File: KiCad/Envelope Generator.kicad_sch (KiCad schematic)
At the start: 36 parts, among them U10 TL074, U9 TL074

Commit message: routed the filter, updated 0201 footprints to 0402
JLCPCB's economy PCBA has a footprint bottom limit of 0402 imperial
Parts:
- R54, R55, R57, R58, R59, R63, R64, R65: footprint Resistor_SMD:R_0201_0603Metric -> Resistor_SMD:R_0402_1005Metric
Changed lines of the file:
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@@
 			)
 		)
-		(property "Footprint" "Resistor_SMD:R_0201_0603Metric"
+		(property "Footprint" "Resistor_SMD:R_0402_1005Metric"
 			(at 50.546 96.774 90)
 			(hide yes)
@@
 			)
 		)
-		(property "Footprint" "Resistor_SMD:R_0201_0603Metric"
+		(property "Footprint" "Resistor_SMD:R_0402_1005Metric"
 			(at 89.916 152.654 90)
 			(hide yes)
@@
 			)
 		)
-		(property "Footprint" "Resistor_SMD:R_0201_0603Metric"
+		(property "Footprint" "Resistor_SMD:R_0402_1005Metric"
 			(at 48.514 40.894 90)
 			(hide yes)
@@
 			)
 		)
-		(property "Footprint" "Resistor_SMD:R_0201_0603Metric"
+		(property "Footprint" "Resistor_SMD:R_0402_1005Metric"
 			(at 35.306 96.774 90)
 			(hide yes)
@@
 			)
 		)
-		(property "Footprint" "Resistor_SMD:R_0201_0603Metric"
+		(property "Footprint" "Resistor_SMD:R_0402_1005Metric"
 			(at 50.546 152.654 90)
 			(hide yes)
@@
 			)
 		)
-		(property "Footprint" "Resistor_SMD:R_0201_0603Metric"
+		(property "Footprint" "Resistor_SMD:R_0402_1005Metric"
 			(at 38.354 40.894 90)
 			(hide yes)
@@
 			)
 		)
-		(property "Footprint" "Resistor_SMD:R_0201_0603Metric"
+		(property "Footprint" "Resistor_SMD:R_0402_1005Metric"
 			(at 89.916 96.774 90)
 			(hide yes)
@@
 			)
 		)
-		(property "Footprint" "Resistor_SMD:R_0201_0603Metric"
+		(property "Footprint" "Resistor_SMD:R_0402_1005Metric"
 			(at 35.306 152.654 90)
 			(hide yes)

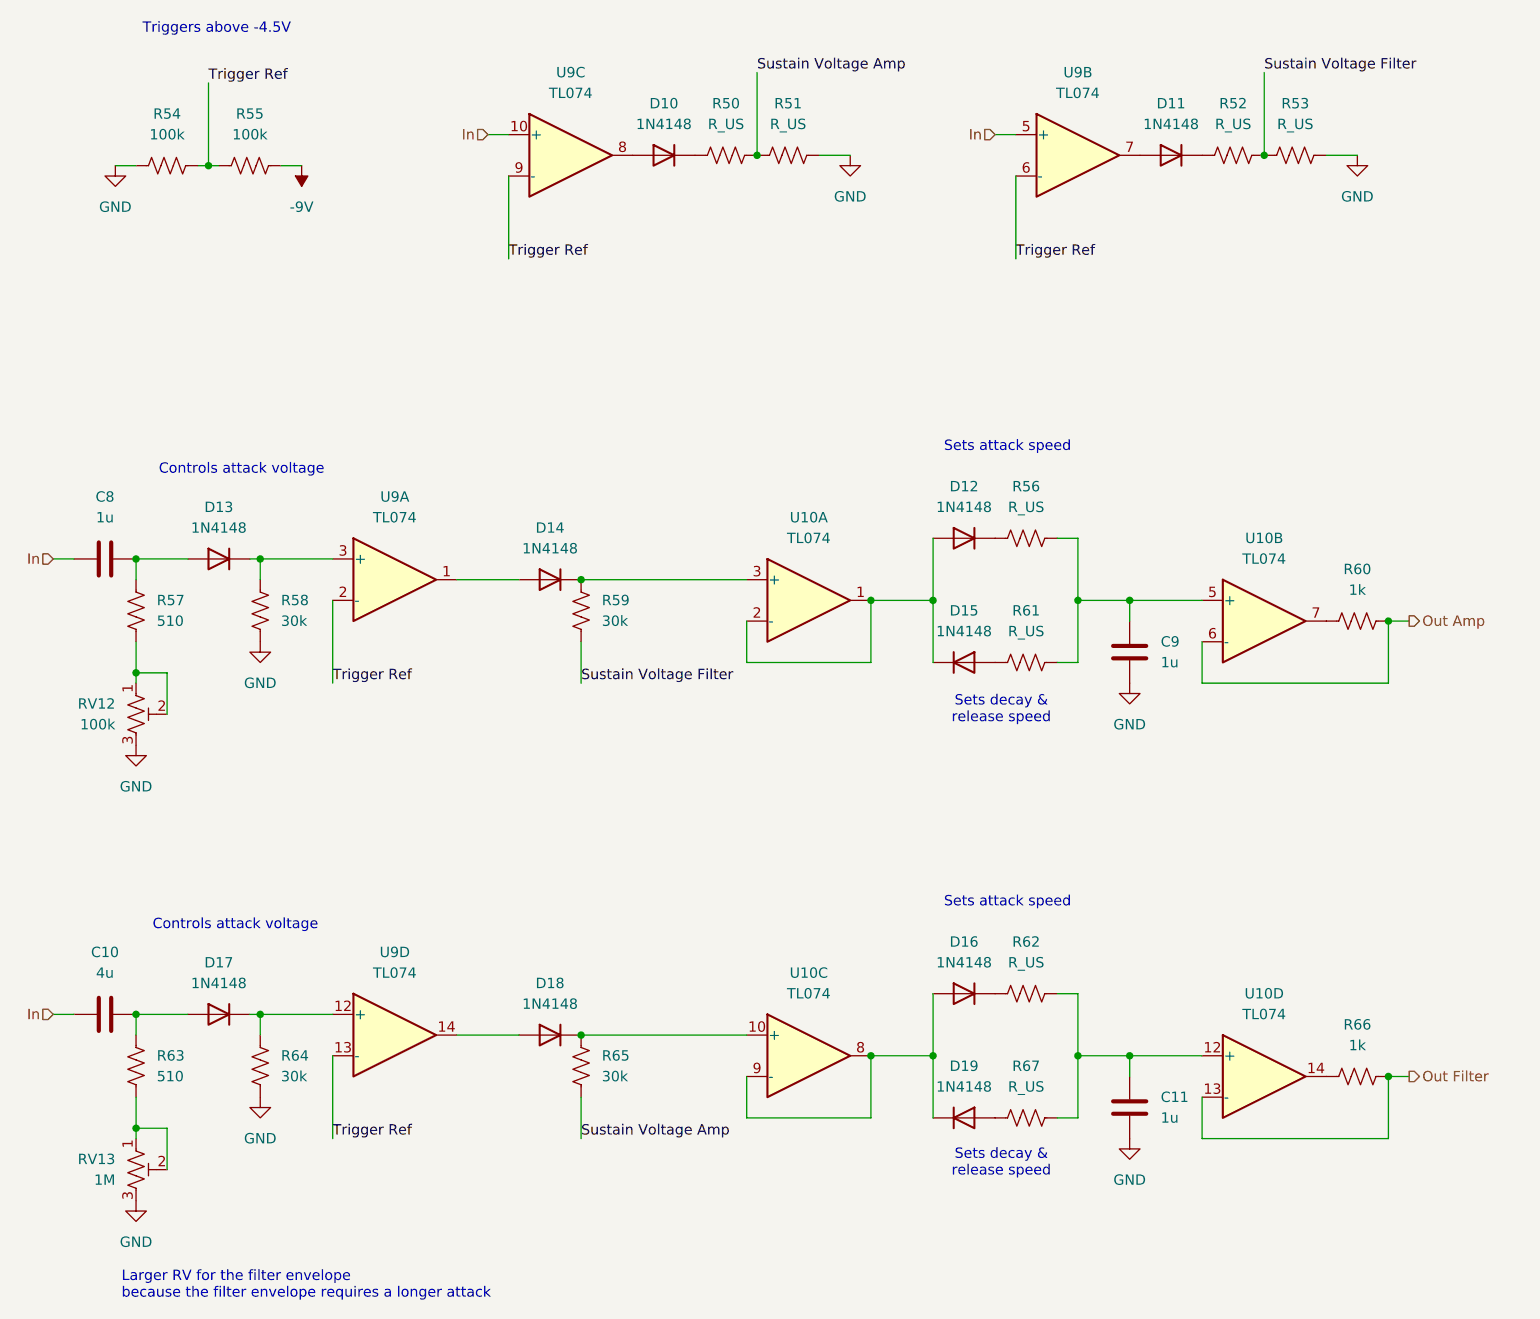
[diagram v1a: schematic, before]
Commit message: placed and routed envelope core
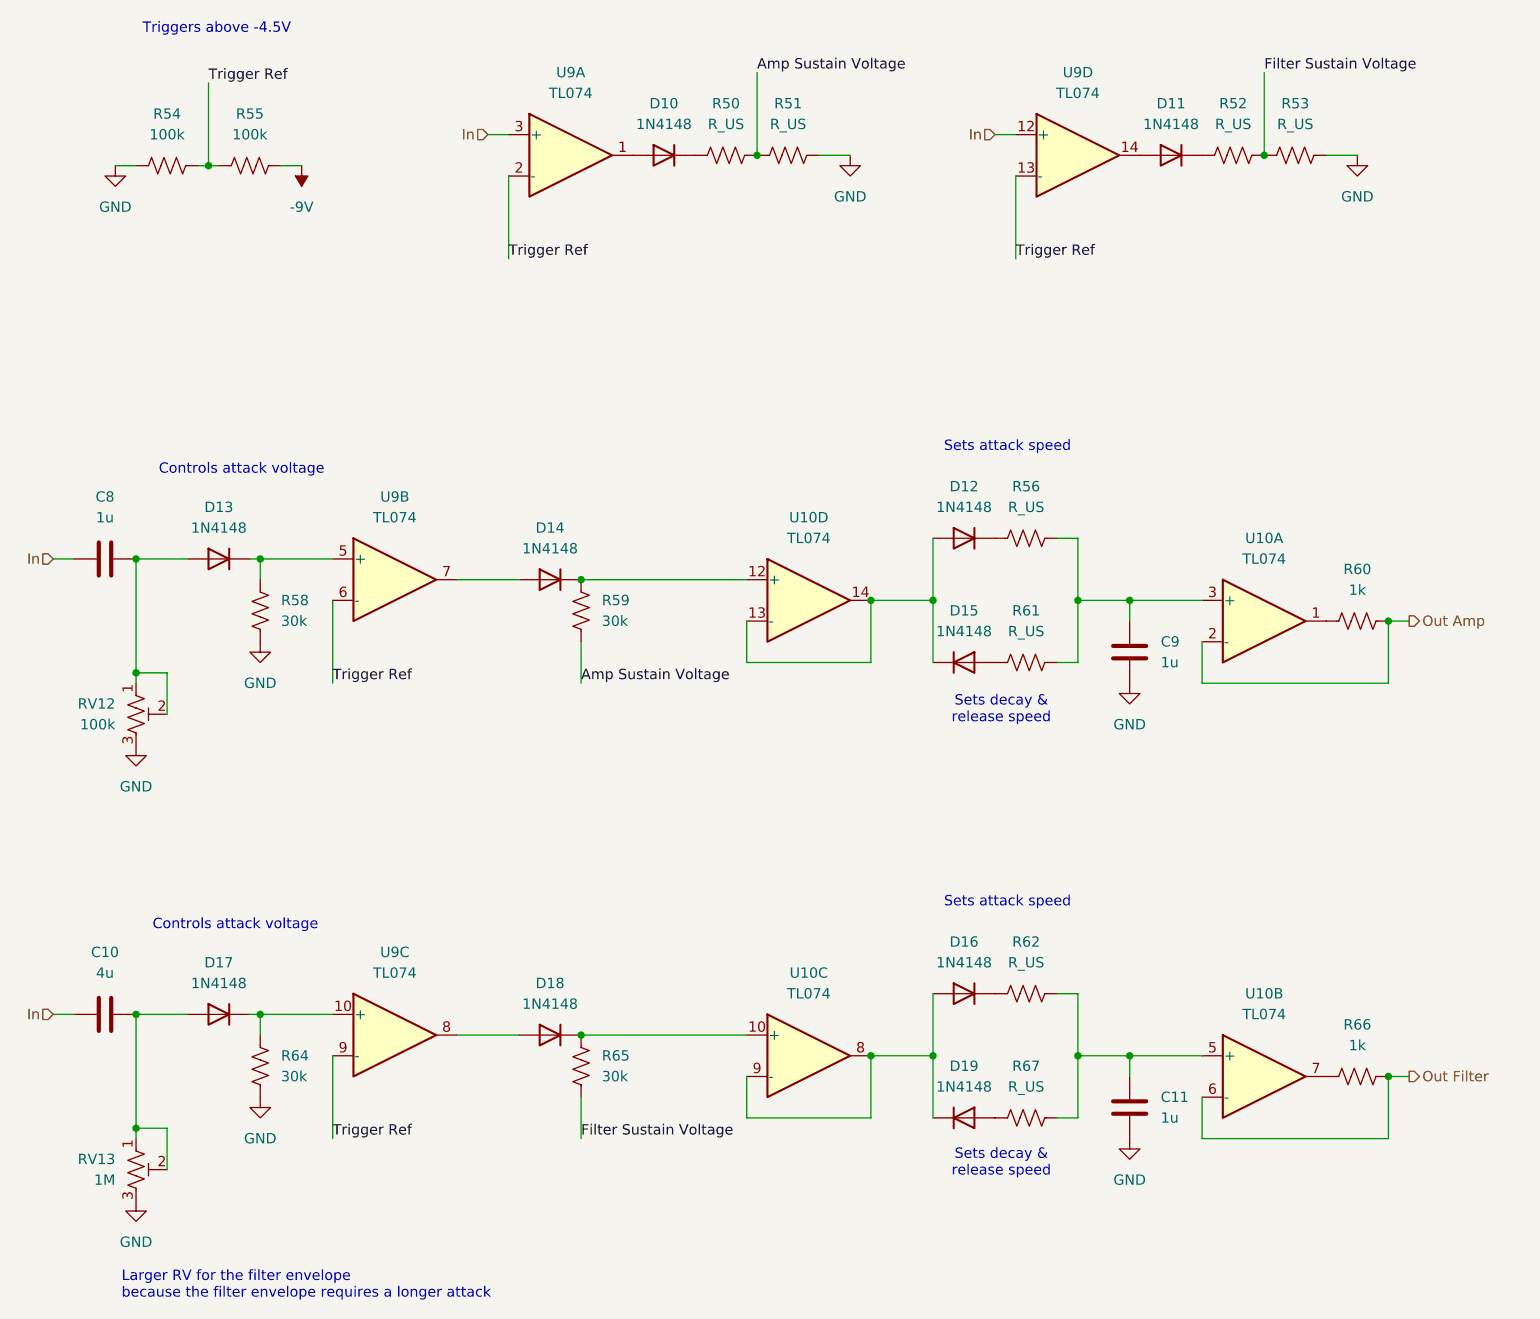
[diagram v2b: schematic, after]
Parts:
- removed R57, R63: 510, Resistor_SMD:R_0402_1005Metric, symbol Device:R_US
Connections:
- net In: now also U9.12 (+), U9.3 (+); no longer U9.10 (+), U9.5 (+)
- net Out Amp: now also U10.2 (-); no longer U10.6 (-)
- net Out Filter: now also U10.6 (-); no longer U10.13 (-)
- net Trigger Ref: now also U9.13 (-), U9.2 (-), U9.6 (-), U9.9 (-); no longer U9.13 (-), U9.2 (-), U9.6 (-), U9.9 (-)
- net at C11.2, R62.2, R67.2: now also U10.5 (+); no longer U10.12 (+)
- net at C9.2, R56.2, R61.2: now also U10.3 (+); no longer U10.5 (+)
- net at C10.2, D17.2 (A): now also RV13.1, RV13.2
- net at D18.2 (A): now also U9.8; no longer U9.14
- net at D10.2 (A): now also U9.1; no longer U9.8
- net at R66.1: now also U10.7; no longer U10.14
- net at D13.1 (K), R58.1: now also U9.5 (+); no longer U9.3 (+)
- net at D12.2 (A), D15.1 (K): now also U10.13 (-), U10.14; no longer U10.1, U10.2 (-)
- net at C8.2, D13.2 (A): now also RV12.1, RV12.2
- net at D17.1 (K), R64.1: now also U9.10 (+); no longer U9.12 (+)
- net at R60.1: now also U10.1; no longer U10.7
- net at D14.1 (K), R59.1: now also U10.12 (+); no longer U10.3 (+)
- net at D14.2 (A): now also U9.7; no longer U9.1
- net at D11.2 (A): now also U9.14; no longer U9.7
- net Sustain Voltage Amp renamed Amp Sustain Voltage
- net Amp Sustain Voltage: now also R59.2; no longer R65.2
- net Sustain Voltage Filter renamed Filter Sustain Voltage
- net Filter Sustain Voltage: now also R65.2; no longer R59.2
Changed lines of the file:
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@@
 	)
 	(junction
-		(at 34.29 104.14)
+		(at 149.86 151.13)
 		(diameter 0)
 		(color 0 0 0 0)
 	)
 	(junction
-		(at 149.86 151.13)
+		(at 88.9 148.59)
 		(diameter 0)
 		(color 0 0 0 0)
 	)
 	(junction
-		(at 88.9 148.59)
+		(at 132.08 151.13)
 		(diameter 0)
 		(color 0 0 0 0)
 	)
 	(junction
-		(at 132.08 151.13)
+		(at 34.29 104.14)
 		(diameter 0)
 		(color 0 0 0 0)
@@
 	(wire
 		(pts
-			(xy 34.29 148.59) (xy 34.29 146.05)
-		)
-		(stroke
-			(width 0)
-			(type default)
-		)
-	)
-	(wire
-		(pts
 			(xy 156.21 151.13) (xy 165.1 151.13)
 		)
@@
 	(wire
 		(pts
-			(xy 34.29 92.71) (xy 34.29 90.17)
+			(xy 34.29 146.05) (xy 34.29 160.02)
+		)
+		(stroke
+			(width 0)
+			(type default)
+		)
+	)
+	(wire
+		(pts
+			(xy 34.29 90.17) (xy 34.29 104.14)
 		)
 		(stroke
@@
 	(wire
 		(pts
-			(xy 34.29 100.33) (xy 34.29 104.14)
-		)
-		(stroke
-			(width 0)
-			(type default)
-		)
-	)
-	(wire
-		(pts
 			(xy 34.29 160.02) (xy 34.29 161.29)
 		)
@@
 	(wire
 		(pts
-			(xy 34.29 156.21) (xy 34.29 160.02)
-		)
-		(stroke
-			(width 0)
-			(type default)
-		)
-	)
-	(wire
-		(pts
 			(xy 149.86 95.25) (xy 149.86 102.87)
 		)
@@
 		)
 	)
-	(label "Sustain Voltage Amp"
-		(at 88.9 161.29 0)
+	(label "Trigger Ref"
+		(at 142.24 53.34 0)
 		(effects
 			(font
@@
 	)
 	(label "Trigger Ref"
-		(at 142.24 53.34 0)
+		(at 80.01 53.34 0)
 		(effects
 			(font
@@
 		)
 	)
-	(label "Sustain Voltage Amp"
-		(at 110.49 30.48 0)
+	(label "Amp Sustain Voltage"
+		(at 88.9 105.41 0)
 		(effects
 			(font
@@
 		)
 	)
-	(label "Trigger Ref"
-		(at 80.01 53.34 0)
+	(label "Filter Sustain Voltage"
+		(at 88.9 161.29 0)
 		(effects
 			(font
@@
 		)
 	)
-	(label "Sustain Voltage Filter"
-		(at 88.9 105.41 0)
+	(label "Amp Sustain Voltage"
+		(at 110.49 30.48 0)
 		(effects
 			(font
@@
 		)
 	)
-	(label "Sustain Voltage Filter"
+	(label "Filter Sustain Voltage"
 		(at 172.72 30.48 0)
 		(effects
@@
 		(lib_id "Amplifier_Operational:TL074")
 		(at 87.63 40.64 0)
-		(unit 3)
+		(unit 1)
 		(body_style 1)
 		(exclude_from_sim no)
@@
 				(path "/931827f3-33b7-460f-8885-7db258da2648/77fe3443-32fb-46cd-8502-6f8d1ae6ff63"
 					(reference "U9")
-					(unit 3)
+					(unit 1)
 				)
 			)
@@
 		(lib_id "Amplifier_Operational:TL074")
 		(at 172.72 153.67 0)
-		(unit 4)
+		(unit 2)
 		(body_style 1)
 		(exclude_from_sim no)
@@
 				(path "/931827f3-33b7-460f-8885-7db258da2648/77fe3443-32fb-46cd-8502-6f8d1ae6ff63"
 					(reference "U10")
-					(unit 4)
+					(unit 2)
 				)
 			)
@@
 	(symbol
 		(lib_id "Device:R_US")
-		(at 34.29 96.52 0)
-		(unit 1)
-		(body_style 1)
-		(exclude_from_sim no)
-		(in_bom yes)
-		(on_board yes)
-		(in_pos_files yes)
-		(dnp no)
-		(fields_autoplaced yes)
-		(property "Reference" "R57"
-			(at 36.83 95.2499 0)
-			(show_name no)
-			(do_not_autoplace no)
-			(effects
-				(font
-					(size 1.27 1.27)
-				)
-				(justify left)
-			)
-		)
-		(property "Value" "510"
-			(at 36.83 97.7899 0)
-			(show_name no)
-			(do_not_autoplace no)
-			(effects
-				(font
-					(size 1.27 1.27)
-				)
-				(justify left)
-			)
-		)
-		(property "Footprint" "Resistor_SMD:R_0402_1005Metric"
-			(at 35.306 96.774 90)
-			(hide yes)
-			(show_name no)
-			(do_not_autoplace no)
-			(effects
-				(font
-					(size 1.27 1.27)
-				)
-			)
-		)
-		(property "Datasheet" ""
-			(at 34.29 96.52 0)
-			(hide yes)
-			(show_name no)
-			(do_not_autoplace no)
-			(effects
-				(font
-					(size 1.27 1.27)
-				)
-			)
-		)
-		(property "Description" "Resistor, US symbol"
-			(at 34.29 96.52 0)
-			(hide yes)
-			(show_name no)
-			(do_not_autoplace no)
-			(effects
-				(font
-					(size 1.27 1.27)
-				)
-			)
-		)
-		(pin "2"
-		)
-		(pin "1"
-		)
-		(instances
-			(project "Electronic Trombone"
-				(path "/931827f3-33b7-460f-8885-7db258da2648/77fe3443-32fb-46cd-8502-6f8d1ae6ff63"
-					(reference "R57")
-					(unit 1)
-				)
-			)
-		)
-	)
-	(symbol
-		(lib_id "Device:R_US")
 		(at 49.53 152.4 0)
 		(unit 1)
@@
 		(lib_id "Amplifier_Operational:TL074")
 		(at 172.72 97.79 0)
-		(unit 2)
+		(unit 1)
 		(body_style 1)
 		(exclude_from_sim no)
@@
 				(path "/931827f3-33b7-460f-8885-7db258da2648/77fe3443-32fb-46cd-8502-6f8d1ae6ff63"
 					(reference "U10")
-					(unit 2)
+					(unit 1)
 				)
 			)
@@
 		(lib_id "Amplifier_Operational:TL074")
 		(at 149.86 40.64 0)
-		(unit 2)
+		(unit 4)
 		(body_style 1)
 		(exclude_from_sim no)
@@
 				(path "/931827f3-33b7-460f-8885-7db258da2648/77fe3443-32fb-46cd-8502-6f8d1ae6ff63"
 					(reference "U9")
-					(unit 2)
+					(unit 4)
 				)
 			)
@@
 		(lib_id "Amplifier_Operational:TL074")
 		(at 66.04 148.59 0)
-		(unit 4)
+		(unit 3)
 		(body_style 1)
 		(exclude_from_sim no)
@@
 				(path "/931827f3-33b7-460f-8885-7db258da2648/77fe3443-32fb-46cd-8502-6f8d1ae6ff63"
 					(reference "U9")
-					(unit 4)
+					(unit 3)
 				)
 			)
@@
 	)
 	(symbol
-		(lib_id "Device:R_US")
-		(at 34.29 152.4 0)
-		(unit 1)
-		(body_style 1)
-		(exclude_from_sim no)
-		(in_bom yes)
-		(on_board yes)
-		(in_pos_files yes)
-		(dnp no)
-		(fields_autoplaced yes)
-		(property "Reference" "R63"
-			(at 36.83 151.1299 0)
-			(show_name no)
-			(do_not_autoplace no)
-			(effects
-				(font
-					(size 1.27 1.27)
-				)
-				(justify left)
-			)
-		)
-		(property "Value" "510"
-			(at 36.83 153.6699 0)
-			(show_name no)
-			(do_not_autoplace no)
-			(effects
-				(font
-					(size 1.27 1.27)
-				)
-				(justify left)
-			)
-		)
-		(property "Footprint" "Resistor_SMD:R_0402_1005Metric"
-			(at 35.306 152.654 90)
-			(hide yes)
-			(show_name no)
-			(do_not_autoplace no)
-			(effects
-				(font
-					(size 1.27 1.27)
-				)
-			)
-		)
-		(property "Datasheet" ""
-			(at 34.29 152.4 0)
-			(hide yes)
-			(show_name no)
-			(do_not_autoplace no)
-			(effects
-				(font
-					(size 1.27 1.27)
-				)
-			)
-		)
-		(property "Description" "Resistor, US symbol"
-			(at 34.29 152.4 0)
-			(hide yes)
-			(show_name no)
-			(do_not_autoplace no)
-			(effects
-				(font
-					(size 1.27 1.27)
-				)
-			)
-		)
-		(pin "2"
-		)
-		(pin "1"
-		)
-		(instances
-			(project "Electronic Trombone"
-				(path "/931827f3-33b7-460f-8885-7db258da2648/77fe3443-32fb-46cd-8502-6f8d1ae6ff63"
-					(reference "R63")
-					(unit 1)
-				)
-			)
-		)
-	)
-	(symbol
 		(lib_id "Amplifier_Operational:TL074")
 		(at 116.84 95.25 0)
-		(unit 1)
+		(unit 4)
 		(body_style 1)
 		(exclude_from_sim no)
@@
 				(path "/931827f3-33b7-460f-8885-7db258da2648/77fe3443-32fb-46cd-8502-6f8d1ae6ff63"
 					(reference "U10")
-					(unit 1)
+					(unit 4)
 				)
 			)
@@
 		(lib_id "Amplifier_Operational:TL074")
 		(at 66.04 92.71 0)
-		(unit 1)
+		(unit 2)
 		(body_style 1)
 		(exclude_from_sim no)
@@
 				(path "/931827f3-33b7-460f-8885-7db258da2648/77fe3443-32fb-46cd-8502-6f8d1ae6ff63"
 					(reference "U9")
-					(unit 1)
+					(unit 2)
 				)
 			)

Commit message: all SMD are 0603 (imperial) now, started rerouting all traces
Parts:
- R54, R55, R58, R59, R60, R64, R65, R66: footprint Resistor_SMD:R_0402_1005Metric -> Resistor_SMD:R_0603_1608Metric
